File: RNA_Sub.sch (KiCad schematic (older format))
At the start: 67 parts, among them J5 AudioJack4, SW12S1 SW_Push_45deg, SW13S1 SW_Push_45deg, SW14S1 SW_Push_45deg, SW15S1 SW_Push_45deg, SW16S1 SW_Push_45deg, SW17S1 SW_Push_45deg, SW22S1 SW_Push_45deg, SW23S1 SW_Push_45deg, SW24S1 SW_Push_45deg, SW25S1 SW_Push_45deg, SW26S1 SW_Push_45deg, SW27S1 SW_Push_45deg, SW32S1 SW_Push_45deg, SW33S1 SW_Push_45deg, SW34S1 SW_Push_45deg, SW35S1 SW_Push_45deg, SW36S1 SW_Push_45deg, SW37S1 SW_Push_45deg, SW41S1 SW_Push_45deg, SW42S1 SW_Push_45deg, SW43S1 SW_Push_45deg, SW44S1 SW_Push_45deg, SW45S1 SW_Push_45deg, SW46S1 SW_Push_45deg, SW47S1 SW_Push_45deg, SW51S1 SW_Push_45deg, SW52S1 SW_Push_45deg, SW53S1 SW_Push_45deg, SW54S1 SW_Push_45deg, SW55S1 SW_Push_45deg, SW56S1 SW_Push_45deg, SW57S1 SW_Push_45deg, U4 MCP23017_SS

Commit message: update annotation
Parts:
- renumbered C8 to C9, D41S1 to D34, D51S1 to D35, D12S1 to D36, D22S1 to D37, D32S1 to D38, D42S1 to D39, D52S1 to D40, D13S1 to D41, D23S1 to D42, D33S1 to D43, D43S1 to D44, D53S1 to D45, D14S1 to D46, D24S1 to D47, D34S1 to D48, D44S1 to D49, D54S1 to D50, D15S1 to D51, D25S1 to D52, D35S1 to D53, D45S1 to D54, D55S1 to D55, D16S1 to D56, D26S1 to D57, D36S1 to D58, D46S1 to D59, D56S1 to D60, D17S1 to D61, D27S1 to D62, D37S1 to D63, D47S1 to D64, D57S1 to D65, SW41S1 to SW35, SW51S1 to SW36, SW12S1 to SW37, SW22S1 to SW38, SW32S1 to SW39, SW42S1 to SW40, SW52S1 to SW41, SW13S1 to SW42, SW23S1 to SW43, SW33S1 to SW44, SW43S1 to SW45, SW53S1 to SW46, SW14S1 to SW47, SW24S1 to SW48, SW34S1 to SW49, SW44S1 to SW50, SW54S1 to SW51, SW15S1 to SW52, SW25S1 to SW53, SW35S1 to SW54, SW45S1 to SW55, SW55S1 to SW56, SW16S1 to SW57, SW26S1 to SW58, SW36S1 to SW59, SW46S1 to SW60, SW56S1 to SW61, SW17S1 to SW62, SW27S1 to SW63, SW37S1 to SW64, SW47S1 to SW65, SW57S1 to SW66, U4 to U5

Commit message: modify module
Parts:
- C9: value C_Small -> 100n
- D34, D35, D36, D37, D38, D39, D40, D41, D42, D43, D44, D45, D46, D47, D48, D49, D50, D51, D52, D53, D54, D55, D56, D57, D58, D59, D60, D61, D62, D63, D64, D65: value D_Small -> 1N4148W
- J5: value AudioJack4 -> SM04B-SRSS-TB(LF)(SN)
- SW35, SW36, SW37, SW38, SW39, SW40, SW41, SW42, SW43, SW44, SW45, SW46, SW47, SW48, SW49, SW50, SW51, SW52, SW53, SW54, SW55, SW56, SW57, SW58, SW59, SW60, SW61, SW62, SW63, SW64, SW65, SW66: value SW_Push_45deg -> CPG135001S30

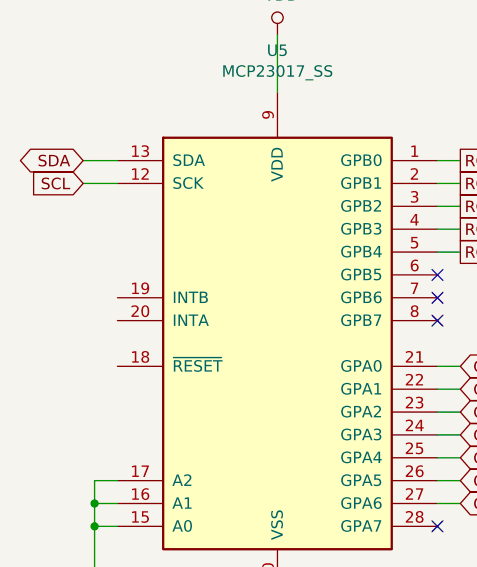
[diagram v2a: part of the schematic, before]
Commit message: chenge microcontroller from STM32L433CCT to STM32F072BCT
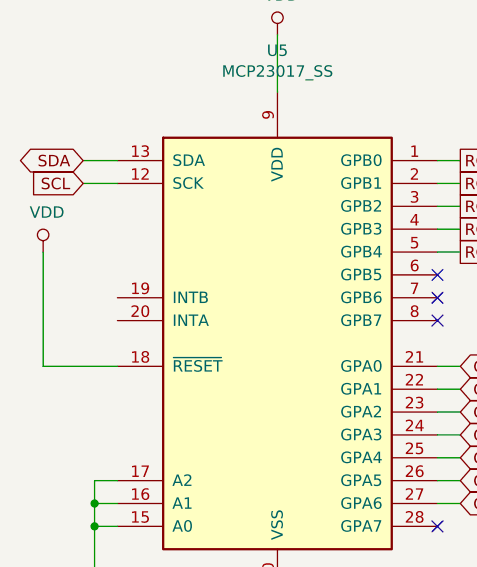
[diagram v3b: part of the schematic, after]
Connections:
- net VDD: now also U5.18 (~RESET~)
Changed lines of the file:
@@
 Wire Wire Line
 	1200 3100 1200 3300
+$Comp
+L power:VDD #PWR0133
+U 1 1 5DEC7E55
+P 975 1900
+F 0 "#PWR0133" H 975 1750 50  0001 C CNN
+F 1 "VDD" H 992 2073 50  0000 C CNN
+F 2 "" H 975 1900 50  0001 C CNN
+F 3 "" H 975 1900 50  0001 C CNN
+	1    975  1900
+	1    0    0    -1
+$EndComp
+Wire Wire Line
+	1300 2400 975  2400
+Wire Wire Line
+	975  2400 975  1900
 $EndSCHEMATC

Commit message: add pull-up resistor for NRST
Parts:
- removed U5: MCP23017_SS, Package_SO:SSOP-28_5.3x10.2mm_P0.65mm, symbol Interface_Expansion:MCP23017_SS
- added C10: 22n, Capacitor_SMD:C_0603_1608Metric, symbol Device:C_Small
- added R7: 10k, Resistor_SMD:R_0603_1608Metric, symbol Device:R_Small
- added U5: PCA9555PW, Package_SO:TSSOP-24_4.4x7.8mm_P0.65mm, symbol Interface_Expansion:PCA9555PW
- D34, D35, D36, D37, D38, D39, D40, D41, D42, D43, D44, D45, D46, D47, D48, D49, D50, D51, D52, D53, D54, D55, D56, D57, D58, D59, D60, D61, D62, D63, D64, D65: LCSC_Parts_No (none) -> C81598
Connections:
- net COL1S: now also U5.4 (IO0_0)
- net COL2S: now also U5.5 (IO0_1)
- net COL3S: now also U5.6 (IO0_2)
- net COL4S: now also U5.7 (IO0_3)
- net COL5S: now also U5.8 (IO0_4)
- net COL6S: now also U5.9 (IO0_5)
- net COL7S: now also U5.10 (IO0_6)
- net GND: now also C10.2, U5.2 (A1), U5.21 (A0), U5.24 (VSS), U5.3 (A2)
- net ROW1S: now also U5.13 (IO1_0)
- net ROW2S: now also U5.14 (IO1_1)
- net ROW3S: now also U5.15 (IO1_2)
- net ROW4S: now also U5.16 (IO1_3)
- net ROW5S: now also U5.17 (IO1_4)
- net SCL: now also U5.22 (SCL)
- net SDA: now also U5.23 (SDA)
- net VDD: now also C10.1, R7.1, U5.12 (VDD)
- new net: R7.2, U5.1 (NINT)
